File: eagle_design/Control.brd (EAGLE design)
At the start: 81.3 x 36.8 mm, 8 parts

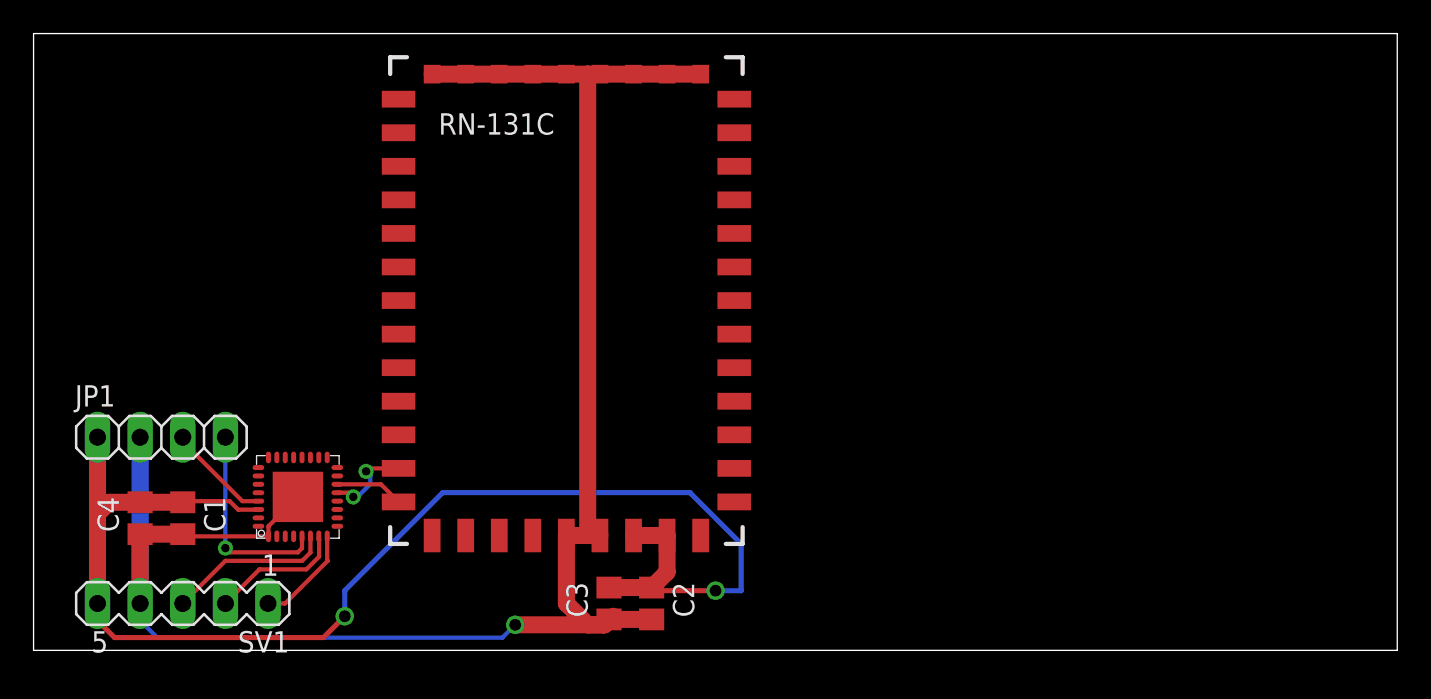
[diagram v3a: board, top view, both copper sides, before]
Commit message: updated schematics
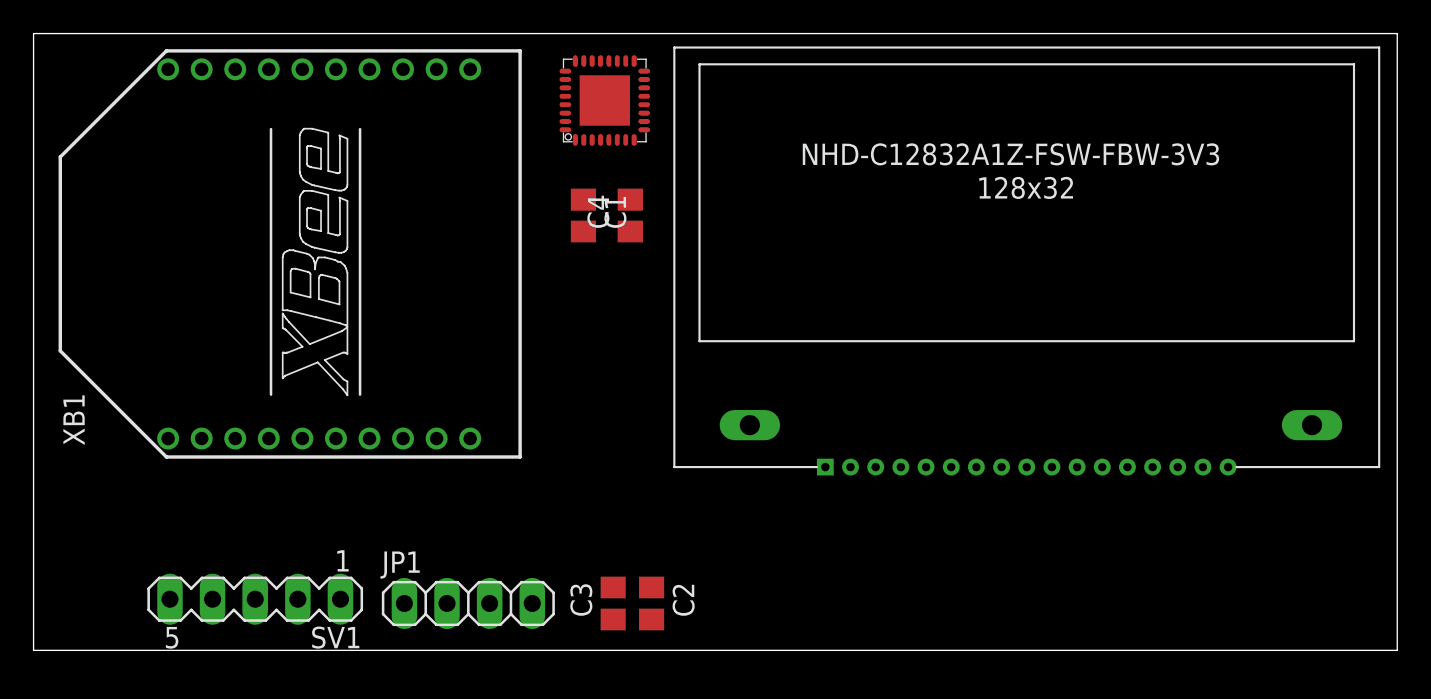
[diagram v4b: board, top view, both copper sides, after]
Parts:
- removed RN-131C: RN-131G, SparkFun:RN-131G
- added U$2: NHD-C12832A1Z-FSW-FBW-3V3, TylersLib:NHD-C12832A1Z-FSW-FBW-3V3
- added XB1: XBEE, maxstream:XBEE
- moved C4 34.3 mm to (35.6, 25.7)
- moved C1 29.9 mm to (32.8, 25.7)
- moved U$1 29.9 mm to (34.0, 32.5)
- moved JP1 20.8 mm to (25.9, 2.54)
- moved SV1 4.33 mm to (13.2, 2.79)
- moved C3 0.25 mm to (34.5, 2.54)
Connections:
- removed net RESET: RN-131C.RESET
- new net SCL: U$1.11, U$2.14
- new net SDA: U$1.10, U$2.13
- net GND: now also XB1.10; no longer RN-131C.3.3-RIN, RN-131C.GND0, RN-131C.GND1, RN-131C.GND2, RN-131C.GND3, RN-131C.GND4, RN-131C.GND5, RN-131C.GND6, RN-131C.GND7, RN-131C.GND8, RN-131C.GND9
- net RN-RX: no longer RN-131C.UART-RX
- net RN-TX: no longer RN-131C.UART-TX
- net VCC: now also XB1.1; no longer RN-131C.VDD-BATT, RN-131C.VDD-IN
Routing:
- net GND: track 110.3 -> 0.00 mm, vias 1 -> 0
- net VCC: track 86.0 -> 0.00 mm, vias 2 -> 0
- net RST: track 12.1 -> 0.00 mm, vias 1 -> 0
- net HEAT: track 9.83 -> 0.00 mm
- net AC: track 7.96 -> 0.00 mm
- net TEST: track 6.24 -> 0.00 mm
- net FAN: track 6.08 -> 0.00 mm
- net RN-RX: track 5.27 -> 0.00 mm, vias 2 -> 0
- net RN-TX: track 4.09 -> 0.00 mm

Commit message: added code, and modified eagle files
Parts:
- removed JP1: (no value), pinhead:1X04
- removed XB1: XBEE, maxstream:XBEE
- added C10, C5, C6, C7, C8, C9: (no value), cap-pan40:C-0603
- added R1: 100 kOhm, Panasonic_By_element14_Batch_1:RESC1608X60N
- added SPW: (no value), pinhead:2X02
- added U$3: NHD-C12832A1Z-FSW-FBW-3V3, TylersLib:NHD-C12832A1Z-FSW-FBW-3V3
- added XB2: RN-XVB1, SteveMarple:XBEE
- C1: device rcl:C0805 -> rcl:C0603K
- C2: value 0.1uF -> 10uF; device rcl:C0805 -> rcl:C0603K
- C3, C4: value 10uF -> (none); device rcl:C0805 -> cap-pan40:C-0603
- SV1: device con-lstb:MA05-1 -> con-lstb:MA03-1
- U$1: value F21X2---RHB32 -> G2XX3---PW28; device TI_MSP430_v16:RHB32 -> TI_MSP430_v16:PW28
- U$2: value NHD-C12832A1Z-FSW-FBW-3V3 -> TEMPERATURE-SENSOR; device TylersLib:NHD-C12832A1Z-FSW-FBW-3V3 -> SparkFun-Sensors:TO-92
- moved U$2 33.2 mm to (29.2, 24.9), turned to 270 degrees
- moved C2 29.8 mm to (39.6, 32.3), flipped to the bottom, turned to 0 degrees
- moved C3 15.8 mm to (41.4, 16.8)
- moved SV1 15.8 mm to (29.0, 3.05), turned to 0 degrees
- moved C4 11.7 mm to (43.2, 16.8)
- moved C1 10.6 mm to (39.6, 33.8), flipped to the bottom, turned to 0 degrees
- moved U$1 8.65 mm to (39.6, 25.9), flipped to the bottom, turned to 270 degrees
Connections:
- net RN-RX renamed P3_2
- net RN-TX renamed P3_3
- new net A0: U$1.8, U$3.15
- new net CS: U$1.9, U$3.17
- new net N$1: C3.2, U$3.1
- new net N$10: C9.1, U$3.9
- new net N$11: R1.1, U$3.A
- new net N$2: C4.2, U$3.2
- new net N$3: C5.2, U$3.3
- new net N$4: C6.2, U$3.4
- new net N$5: C7.2, U$3.5
- new net N$6: C8.2, U$3.6
- new net N$7: C9.2, U$3.8
- new net N$8: C8.1, U$3.7
- new net N$9: C10.2, U$3.10
- new net P1_3: U$1.5
- new net P1_4: U$1.6
- new net P1_6: U$1.22
- new net P2_0: U$1.10
- new net P2_1: U$1.11
- new net P2_2: U$1.12
- new net P2_3: U$1.16
- new net P2_4: U$1.17
- new net P2_5: U$1.18
- new net P2_6: U$1.27
- new net P2_7: U$1.26
- new net P3_4: U$1.15
- new net P3_5: U$1.19
- new net P3_6: U$1.20
- new net P3_7: U$1.21
- new net RX: U$1.3, XB2.2
- new net TEMP: U$1.2, U$2.2
- new net TX: U$1.4, XB2.3
- net AC: no longer U$1.7
- net FAN: now also SV1.3; no longer SV1.1, U$1.8
- net GND: now also C10.1, C3.1, C4.1, C5.1, C6.1, C7.1, SPW.3, U$1.28, U$2.1, U$3.11, U$3.K, XB2.10; no longer C3.2, C4.2, JP1.2, SV1.4, U$1.1, U$1.TP, XB1.10
- net HEAT: now also SV1.1; no longer SV1.3, U$1.6
- net RST: now also SPW.4, U$1.24; no longer JP1.4, U$1.5
- net SCL: now also U$1.7, U$3.14; no longer U$1.11, U$2.14
- net SDA: now also U$1.23, U$3.13; no longer U$1.10, U$2.13
- net TEST: now also SPW.2, U$1.25; no longer JP1.3, U$1.29
- net VCC: now also R1.2, SPW.1, U$1.1, U$2.3, U$3.12, U$3.16, XB2.1, XB2.5; no longer C3.1, C4.1, JP1.1, SV1.5, U$1.30, XB1.1
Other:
- board size 81.3 x 36.8 mm -> 76.2 x 38 mm

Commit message: finished control board
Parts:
- added SW1: EC12E_SW, switch-alps:ALPS_EC12E_SW
- moved SPW 44.6 mm to (72.4, 21.3), turned to 270 degrees
- moved SV1 44.2 mm to (72.1, 12.4), turned to 270 degrees
- moved U$2 41.1 mm to (67.6, 39.6), flipped to the bottom, turned to 180 degrees
- moved C1 26.6 mm to (61.7, 19.1), flipped to the top
- moved U$1 25.7 mm to (61.7, 12.7), flipped to the top
- moved R1 25.0 mm to (21.5, 6.92)
- moved C2 25.0 mm to (61.7, 20.6), flipped to the top
- moved U$3 18.1 mm to (38.1, 20.3)
- moved C7 16.8 mm to (33.5, 24.4)
- moved C8 16.8 mm to (35.3, 24.4)
- moved C10 16.8 mm to (38.9, 24.4)
- moved C3 16.8 mm to (26.4, 24.4)
- moved C4 16.8 mm to (28.2, 24.4)
- moved C5 16.8 mm to (30.0, 24.4)
- moved C6 16.8 mm to (31.8, 24.4)
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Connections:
- removed net P2_2: U$1.12
- removed net P2_3: U$1.16
- removed net P2_4: U$1.17
- removed net P3_2: U$1.13
- removed net P3_3: U$1.14
- removed net P3_4: U$1.15
- new net A: SW1.B, U$1.13
- new net B: SW1.A, U$1.14
- new net OFF: SW1.E, U$1.12
- net AC: now also U$1.16
- net FAN: now also U$1.15
- net GND: now also SPW.4, SW1.C; no longer SPW.3
- net HEAT: now also U$1.17
- net RST: now also SPW.3; no longer SPW.4
- net TEST: now also SPW.1; no longer SPW.2
- net VCC: now also SPW.2, SW1.D; no longer SPW.1
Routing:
- net RX: track 0.00 -> 45.3 mm
- net TX: track 0.00 -> 44.8 mm
- net SDA: track 0.00 -> 32.2 mm, vias 0 -> 1
- net OFF: track 0.00 -> 30.1 mm
- net TEMP: track 0.00 -> 28.0 mm, vias 0 -> 1
- net GND: track 0.00 -> 23.4 mm, vias 0 -> 1
- net A0: track 0.00 -> 18.1 mm, vias 0 -> 1
- net CS: track 0.00 -> 17.1 mm, vias 0 -> 1
- net SCL: track 0.00 -> 16.9 mm, vias 0 -> 1
- net N$11: track 0.00 -> 15.4 mm
- net A: track 0.00 -> 14.6 mm
- net B: track 0.00 -> 14.1 mm
- net VCC: track 0.00 -> 13.9 mm
- net TEST: track 0.00 -> 11.6 mm
- net RST: track 0.00 -> 10.2 mm
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- added copper zone on layer 16, net GND
- added copper zone on layer 1, net VCC
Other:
- board size 76.2 x 38 mm -> 76.2 x 50.7 mm

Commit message: modification of control board
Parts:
- moved R1 9.75 mm to (20.6, 16.6), turned to 270 degrees
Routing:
- net N$11: track 15.4 -> 4.65 mm
- net VCC: track 13.9 -> 5.35 mm
- net CS: track 17.1 -> 15.2 mm
- net A0: track 18.1 -> 16.3 mm
- net SDA: track 32.2 -> 31.6 mm
